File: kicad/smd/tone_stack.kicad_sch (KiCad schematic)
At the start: 5 parts

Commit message: Mixed SMD/THT variant (kicad/smd, 155x90), JFET pin-number fix, THT fully routed
Build profiles: gen_kicad.py / gen_pcb.py / gen_bom.py take --profile tht|smd.
One schematic source; the smd profile remaps footprints and writes a self-
contained KiCad project to kicad/smd/ (cambridge_reverb_smd.*, lib tables one
level up), sized 155 x 90 mm for the Part 7 safe-bet chassis.

SMD (70 parts): 0805 R (1206 for R_reg2), 1206 C <= 100 nF, 1210 for 120 nF /
1 uF / C_zobel, SMA + SOD-123 diodes, SOT-23 JFETs fitted directly.
Deliberately THT: power parts, all electrolytics (standing cans use less board
than SMD cans), DIP-8 sockets for the TL072s, the three bench-trimmed JFET
source resistors, LED, connectors, test points. Parts area 4560 mm^2 -> 48 % of
the 155x90 usable area (THT 60 %).

SMD board specifics: 6 mm margin, 0.6 mm gap, 3 mm channels, pad row clear of
the corner holes; GND pour on both layers (top pour solid to SMD ground pads
only, router sees just the bottom plane so every SMD ground pad gets a via);
HighCurrent/Power classes 2.0/1.0 mm for this board (errata #11 addendum).
Routed: 165/167 connections, 1 DRC error (starved thermal), 109 vias; the two
open items are listed in PCB-NOTES as GUI touches. Eight router settings and
three pour strategies compared; the committed one is the best of them.

Errata #18 (HIGH): the JFET symbol had 2 = Gate / 3 = Source; onsemi's 2N5457
(TO-92) and MMBF5457 (SOT-23) both number the leads 1 D / 2 S / 3 G, so the THT
board would have swapped gate and source on Q1, Q2, Q_rec. Symbol renumbered,
both boards regenerated. THT board re-routed (also fixed the column balance):
166/166 connections, 0 DRC violations, 66 vias -- fully routed.

Also: bom/bom-smd*.csv (spec notes, no invented P/Ns), production/smd/
bom-jlcpcb.csv + position file + README for JLCPCB assembly of the SMD side;
route_board.py --drop-planes and default via cost 60; docs (PCB-NOTES,
PCB-AUDIT, README, CHANGELOG, errata, availability audit, Part 10, kicad and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
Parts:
- C_cut: footprint Capacitor_THT:C_Disc_D7.5mm_W2.5mm_P5.00mm -> Capacitor_SMD:C_1206_3216Metric
- R_fx_pad: footprint Resistor_THT:R_Axial_DIN0207_L6.3mm_D2.5mm_P5.08mm_Vertical -> Resistor_SMD:R_0805_2012Metric
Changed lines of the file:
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@@
     (pin "3")
     (pin "2")
-    (instances (project "cambridge_reverb" (path "/4dee1173-43e9-4350-8b22-fe413d455f7c" (reference "POT_VOL") (unit 1))))
+    (instances (project "cambridge_reverb" (path "/9c6a2d88-6f3c-4155-9cad-846ea22543df" (reference "POT_VOL") (unit 1))))
   )
   (wire (pts (xy 158.75 52.06999999999999) (xy 156.21 52.06999999999999)) (stroke (width 0) (type default)))
@@
     (property "Reference" "R_fx_pad" (at 166.36999999999998 85.08999999999999 0) (effects (font (size 1.27 1.27)) (justify left)))
     (property "Value" "10k" (at 166.36999999999998 87.63 0) (effects (font (size 1.27 1.27)) (justify left)))
-    (property "Footprint" "Resistor_THT:R_Axial_DIN0207_L6.3mm_D2.5mm_P5.08mm_Vertical" (at 163.82999999999998 92.71 0) (effects (font (size 1.27 1.27)) hide))
+    (property "Footprint" "Resistor_SMD:R_0805_2012Metric" (at 163.82999999999998 92.71 0) (effects (font (size 1.27 1.27)) hide))
     (pin "1")
     (pin "2")
-    (instances (project "cambridge_reverb" (path "/4dee1173-43e9-4350-8b22-fe413d455f7c" (reference "R_fx_pad") (unit 1))))
+    (instances (project "cambridge_reverb" (path "/9c6a2d88-6f3c-4155-9cad-846ea22543df" (reference "R_fx_pad") (unit 1))))
   )
   (wire (pts (xy 158.75 92.71) (xy 156.21 92.71)) (stroke (width 0) (type default)))
@@
     (property "Reference" "C_cut" (at 236.22 44.449999999999996 0) (effects (font (size 1.27 1.27)) (justify left)))
     (property "Value" "10nF" (at 236.22 46.989999999999995 0) (effects (font (size 1.27 1.27)) (justify left)))
-    (property "Footprint" "Capacitor_THT:C_Disc_D7.5mm_W2.5mm_P5.00mm" (at 233.68 52.06999999999999 0) (effects (font (size 1.27 1.27)) hide))
+    (property "Footprint" "Capacitor_SMD:C_1206_3216Metric" (at 233.68 52.06999999999999 0) (effects (font (size 1.27 1.27)) hide))
     (pin "1")
     (pin "2")
-    (instances (project "cambridge_reverb" (path "/4dee1173-43e9-4350-8b22-fe413d455f7c" (reference "C_cut") (unit 1))))
+    (instances (project "cambridge_reverb" (path "/9c6a2d88-6f3c-4155-9cad-846ea22543df" (reference "C_cut") (unit 1))))
   )
   (wire (pts (xy 228.59999999999997 52.06999999999999) (xy 226.06 52.06999999999999)) (stroke (width 0) (type default)))
@@
     (pin "3")
     (pin "2")
-    (instances (project "cambridge_reverb" (path "/4dee1173-43e9-4350-8b22-fe413d455f7c" (reference "POT_TONE") (unit 1))))
+    (instances (project "cambridge_reverb" (path "/9c6a2d88-6f3c-4155-9cad-846ea22543df" (reference "POT_TONE") (unit 1))))
   )
   (wire (pts (xy 274.32 52.06999999999999) (xy 271.78 52.06999999999999)) (stroke (width 0) (type default)))
@@
     (property "Footprint" "cambridge_reverb:TestPoint_THT_D2.0mm_Label" (at 133.35 232.41 0) (effects (font (size 1.27 1.27)) hide))
     (pin "1")
-    (instances (project "cambridge_reverb" (path "/4dee1173-43e9-4350-8b22-fe413d455f7c" (reference "TP_TONE_OUT") (unit 1))))
+    (instances (project "cambridge_reverb" (path "/9c6a2d88-6f3c-4155-9cad-846ea22543df" (reference "TP_TONE_OUT") (unit 1))))
   )
   (wire (pts (xy 133.35 234.95) (xy 133.35 237.48999999999998)) (stroke (width 0) (type default)))

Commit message: Tone stack: Bass + Treble (passive James) with a switchable mid cut (errata #20)
The panel has Bass and Treble pots, but the design carried a single treble-cut
"Tone" substitute -- and the recovered preamp coupling was the 470 pF chime cap
alone, a 1.3 kHz high-pass that passed no bass at all. Replace both:

- C_cpl_out 1 uF full-band coupling from Q2's drain; C_treble 470 pF becomes a
  bright cap across the top of the volume pot.
- Passive James (Thomas-Vox) Bass/Treble network -- the originals' topology,
  asymmetric, more cut than boost, kept over an active Baxandall so the amp
  keeps its character -- driven by a TL074 (IC3: input buffer, x2 make-up,
  gyrator, output buffer) on its own mid-rail VBIAS_3. Both pots 250k lin in
  the original holes.
- MID CUT toggle for honky pickups: R_mid + a switched series-resonant gyrator
  shunt (1.86 H simulated + 22 nF): -9.6 dB at ~800 Hz, Q ~0.6, flat when off,
  no DC across the switch. SW_MID sits in the original line-reverse switch
  hole -- no new panel holes.
- SPICE: ac_tonestack.cir rewritten rail-aware (all IC3 nodes 8.50 V, noon
  -0.21 dB, notch -9.65 dB at 796 Hz); sweep_tonestack.cir sweeps both pots
  and the switch; results committed.

Generator / placer / router:
- OPAMP14 and SW_SPST symbols, VB_3 / TMK test points (28), BOM rows for IC3,
  the DIP-14 socket, POT_BASS/POT_TREB, SW_MID.
- gen_pcb: tighter profiles (THT 1.2 mm gap / 3.5 mm channels, SMD 0.4 mm),
  overflow repair by moving width between columns, small parts kept in
  schematic order on the shelves, tone/preamp column weighted wider, TP cells
  6x4.5 with the courtyard flush to the cell, input-jack pads down the LEFT
  edge on the 155x90 board (the bottom edge is ~9 mm short for 13 groups),
  keepout rule areas (2 mm edge frame + M3 hole squares) exported to the
  router.
- route_board: refuse a board without its .kicad_pro (a copy routed away from
  the project came back with 0.2 mm tracks and 400 DRC errors); prune
  zero-length segments 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
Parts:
- removed C_cut: 10nF, Capacitor_SMD:C_1206_3216Metric, symbol cr_primitives:C
- removed POT_TONE: 100k lin, cambridge_reverb:WirePad_1x03_P2.54mm_D1.2mm, symbol cr_primitives:POT
- added C_byp3: 100nF, Capacitor_SMD:C_1206_3216Metric, symbol cr_primitives:C
- added C_gg: 1.8nF, Capacitor_SMD:C_1206_3216Metric, symbol cr_primitives:C
- added C_j1, C_j2, C_res: 22nF, Capacitor_SMD:C_1206_3216Metric, symbol cr_primitives:C
- added C_j3, C_j4: 2.2nF, Capacitor_SMD:C_1206_3216Metric, symbol cr_primitives:C
- added C_tout: 1uF, Capacitor_SMD:C_1210_3225Metric, symbol cr_primitives:C
- added C_treble: 470pF, Capacitor_SMD:C_1206_3216Metric, symbol cr_primitives:C
- added C_vb3: 47uF/25V, Capacitor_THT:CP_Radial_D6.3mm_P2.50mm, symbol cr_primitives:CP
- added IC3: TL074CN, Package_DIP:DIP-14_W7.62mm, symbol cr_primitives:OPAMP14
- added POT_BASS, POT_TREB: 250k lin, cambridge_reverb:WirePad_1x03_P2.54mm_D1.2mm, symbol cr_primitives:POT
- added R_gL: 4.7k, Resistor_SMD:R_0805_2012Metric, symbol cr_primitives:R
- added R_gg: 220k, Resistor_SMD:R_0805_2012Metric, symbol cr_primitives:R
- added R_inb: 1M, Resistor_SMD:R_0805_2012Metric, symbol cr_primitives:R
- added R_j1, R_j2, R_mid, R_mk1, R_mk2: 10k, Resistor_SMD:R_0805_2012Metric, symbol cr_primitives:R
- added R_j3: 68k, Resistor_SMD:R_0805_2012Metric, symbol cr_primitives:R
- added R_j4: 1k, Resistor_SMD:R_0805_2012Metric, symbol cr_primitives:R
- added R_vb31, R_vb32: 100k, Resistor_SMD:R_0805_2012Metric, symbol cr_primitives:R
- added SW_MID: MID CUT, cambridge_reverb:WirePad_1x02_P2.54mm_D1.2mm, symbol cr_primitives:SW_SPST
- added TP_MK_OUT: TMK, cambridge_reverb:TestPoint_THT_D2.0mm_Label, symbol cr_primitives:TP
- added TP_VBIAS_3: VB_3, cambridge_reverb:TestPoint_THT_D2.0mm_Label, symbol cr_primitives:TP
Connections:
- net GND: now also C_byp3.2, C_vb3.2, IC3.11 (V-), R_vb32.2
- net PREAMP_OUT: now also IC3.3 (IN1+), R_inb.1; no longer POT_VOL.1
- net TONE_OUT: now also C_treble.2
- new net +17V: C_byp3.1, IC3.4 (V+), R_vb31.1
- new net BUF: C_j3.1, IC3.1 (OUT1), IC3.2 (IN1-), R_j1.1
- new net GYA: C_gg.1, C_res.2, R_gL.1
- new net GYO: IC3.8 (OUT3), IC3.9 (IN3-), R_gL.2
- new net GYP: C_gg.2, IC3.10 (IN3+), R_gg.1
- new net JA: C_j1.1, POT_BASS.3, R_j1.2
- new net JB: C_j2.2, POT_BASS.1, R_j2.1
- new net JOUT: IC3.5 (IN2+), R_j3.2, R_j4.2
- new net JTA: C_j3.2, POT_TREB.3
- new net JTB: C_j4.1, POT_TREB.1
- new net JWB: C_j1.2, C_j2.1, POT_BASS.2 (W), R_j3.1
- new net JWT: POT_TREB.2 (W), R_j4.1
- new net MID: IC3.12 (IN4+), R_mid.2, SW_MID.1
- new net MIDSW: C_res.1, SW_MID.2
- new net MKN: IC3.6 (IN2-), R_mk1.2, R_mk2.1
- new net MK_OUT: IC3.7 (OUT2), R_mid.1, R_mk1.1, TP_MK_OUT.1
- new net OBUF: C_tout.1, IC3.13 (IN4-), IC3.14 (OUT4)
- new net VBIAS_3: C_j4.2, C_vb3.1 (+), R_gg.2, R_inb.2, R_j2.2, R_mk2.2, R_vb31.2, R_vb32.1, TP_VBIAS_3.1
- new net VOLTOP: C_tout.2, C_treble.1, POT_VOL.1
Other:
- note added: "TONE -- IC3 TL074. A: input buffer. PASSIVE JAMES bass/treble network (the Thomas-Vox topology: panel Bass + Treble pots; ~flat at noon with a slight bright tilt, bass +-6 dB @100 Hz, treble +6/-16 dB @10 kHz -- more cut than boost, as the originals). B: make-up gain x2 (network loss). C: gyrator MID CUT (-10 dB @ ~790 Hz, Q~0.6, SW_MID toggle in the line-reverse hole). D: output buffer -> Volume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"
- note removed: "TONE -- Volume + passive Vox 'cut' (treble). DESIGNED SUBSTITUTE: original 25-5274-2 tone values not recovered (cross-check #4); response verified in spice/ac_tonestack.cir. Original panel may have had separate Treble/Bass."

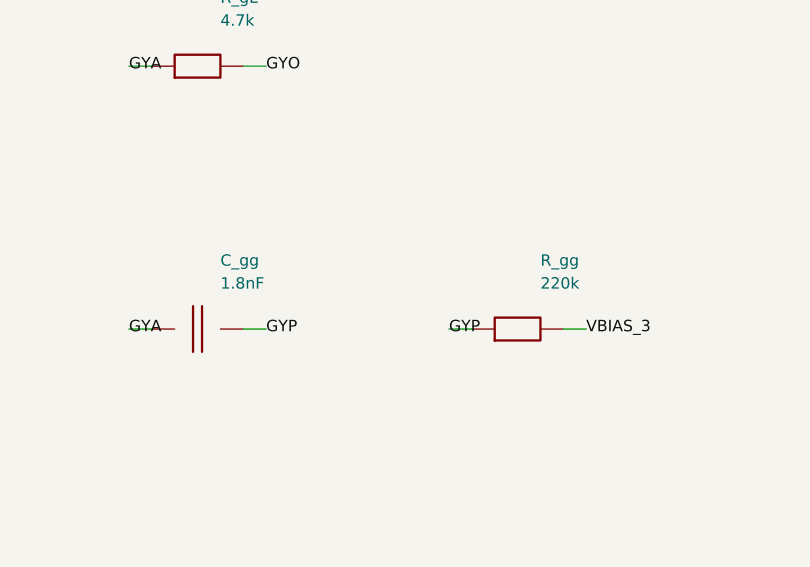
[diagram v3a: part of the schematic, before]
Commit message: Noise, hum, crosstalk and thermal models; three design fixes; JLCPCB rules and cost
New models (docs/06c, spice/): a .noise run of the whole front end including the
LM317's own rail noise, the rail-ripple paths to the speaker, a vactrol-level tremolo
depth model, an electro-thermal LM1875 ladder, and a geometric crosstalk audit of the
routed boards (kicad/gen/crosstalk_audit.py). They found three defects:

- Errata #21 (hum + hiss): the LM1875 bias divider had no bypass (+4 dB ripple to
  speaker, 0.4 Vrms of 100 Hz at idle) and the LM317's 0.5 mV of noise reached the
  0 dB-PSRR JFET stages (23 dB above their floor, SNR 34 dB). Fixed with C_bref +
  R_bias3 on the power amp, C_adj on the regulator, and an RC-decoupled +17V_PRE rail
  for Q1/Q2/Q_rec: hum 408 mV -> 0.3 mV, EIN 37 -> 2.7 uV, SNR 34 -> 57 dB.
- Errata #22 (tremolo depth 1.7 dB): the vactrol LED was returned to ground from a
  mid-rail LFO -> 7 mA DC, a fixed -20 dB pad. LED limiter (2 V swing, LED_rate is one
  limiter LED) + Q_trem 2N3904/MMBT3904 emitter follower AC-coupled from the depth
  pot -> 15 dB depth, 0.8 dB insertion loss.
- Errata #23 (fab): stock TO-92 and the LM1875 footprint were under JLCPCB's 0.18 mm
  annular-ring minimum -> TO-92_Inline_Wide and 1.5 mm LM1875 pads; both .kicad_pro
  carry JLC's 2-layer limits as DRC constraints. Cost: all SMD caps 1206 (basic
  library), "(opt)" MRB caps DNP, gyrator on E24 values (same 1.86 H): 7 -> 2
  extended part types, ~$32 -> ~$17 assembly for five boards (kicad/gen/jlc_cost.py);
  three fiducials on the SMD board.

Crosstalk -> two routing rules (.kicad_dru: HighCurrent 0.6/0.4 mm and TankDrive
1.2/0.8 mm from signal copper, THT/SMD) that route_board.py also hands the router as
class clearances; keepout rule areas along the edge and around the mounting holes.
Thermal: Part 5's <= 2.5 K/W heatsink confirmed with numbers (Tj 97 C at 40 C ambient,
worst-case sine; 8-10 K/W clip-ons reach shutdown).

Placer: short parts stack beside tall ones i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
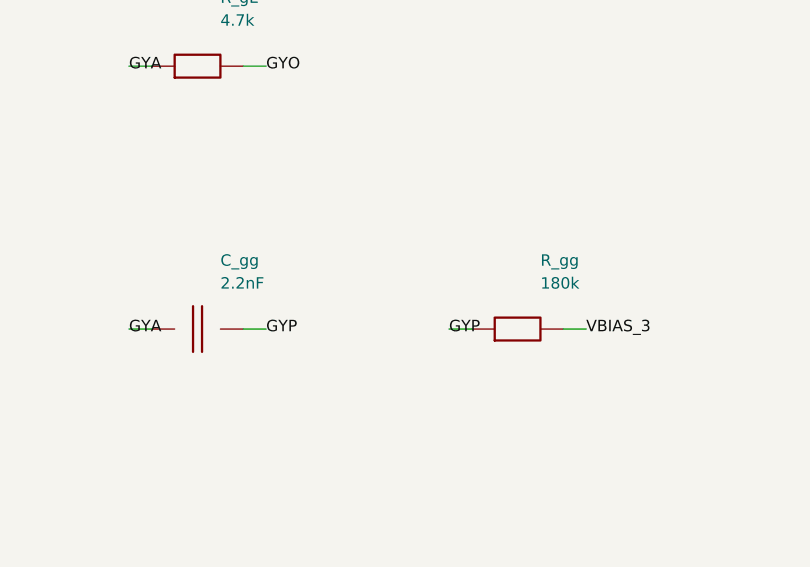
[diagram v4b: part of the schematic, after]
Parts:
- C_gg: value 1.8nF -> 2.2nF
- C_tout: footprint Capacitor_SMD:C_1210_3225Metric -> Capacitor_SMD:C_1206_3216Metric
- R_gg: value 220k -> 180k
